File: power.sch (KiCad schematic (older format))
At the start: 70 parts, among them J6 7-17 V IN, Q1 DMP3099L-7, SW7 JS202011SCQN, U1 ICE40HX4K-TQ144, U10 MAX40200AUK, U12 TPS562201, U15 MAX40200AUK, U6 TLV62568APDRLR, U7 TLV62568APDRLR

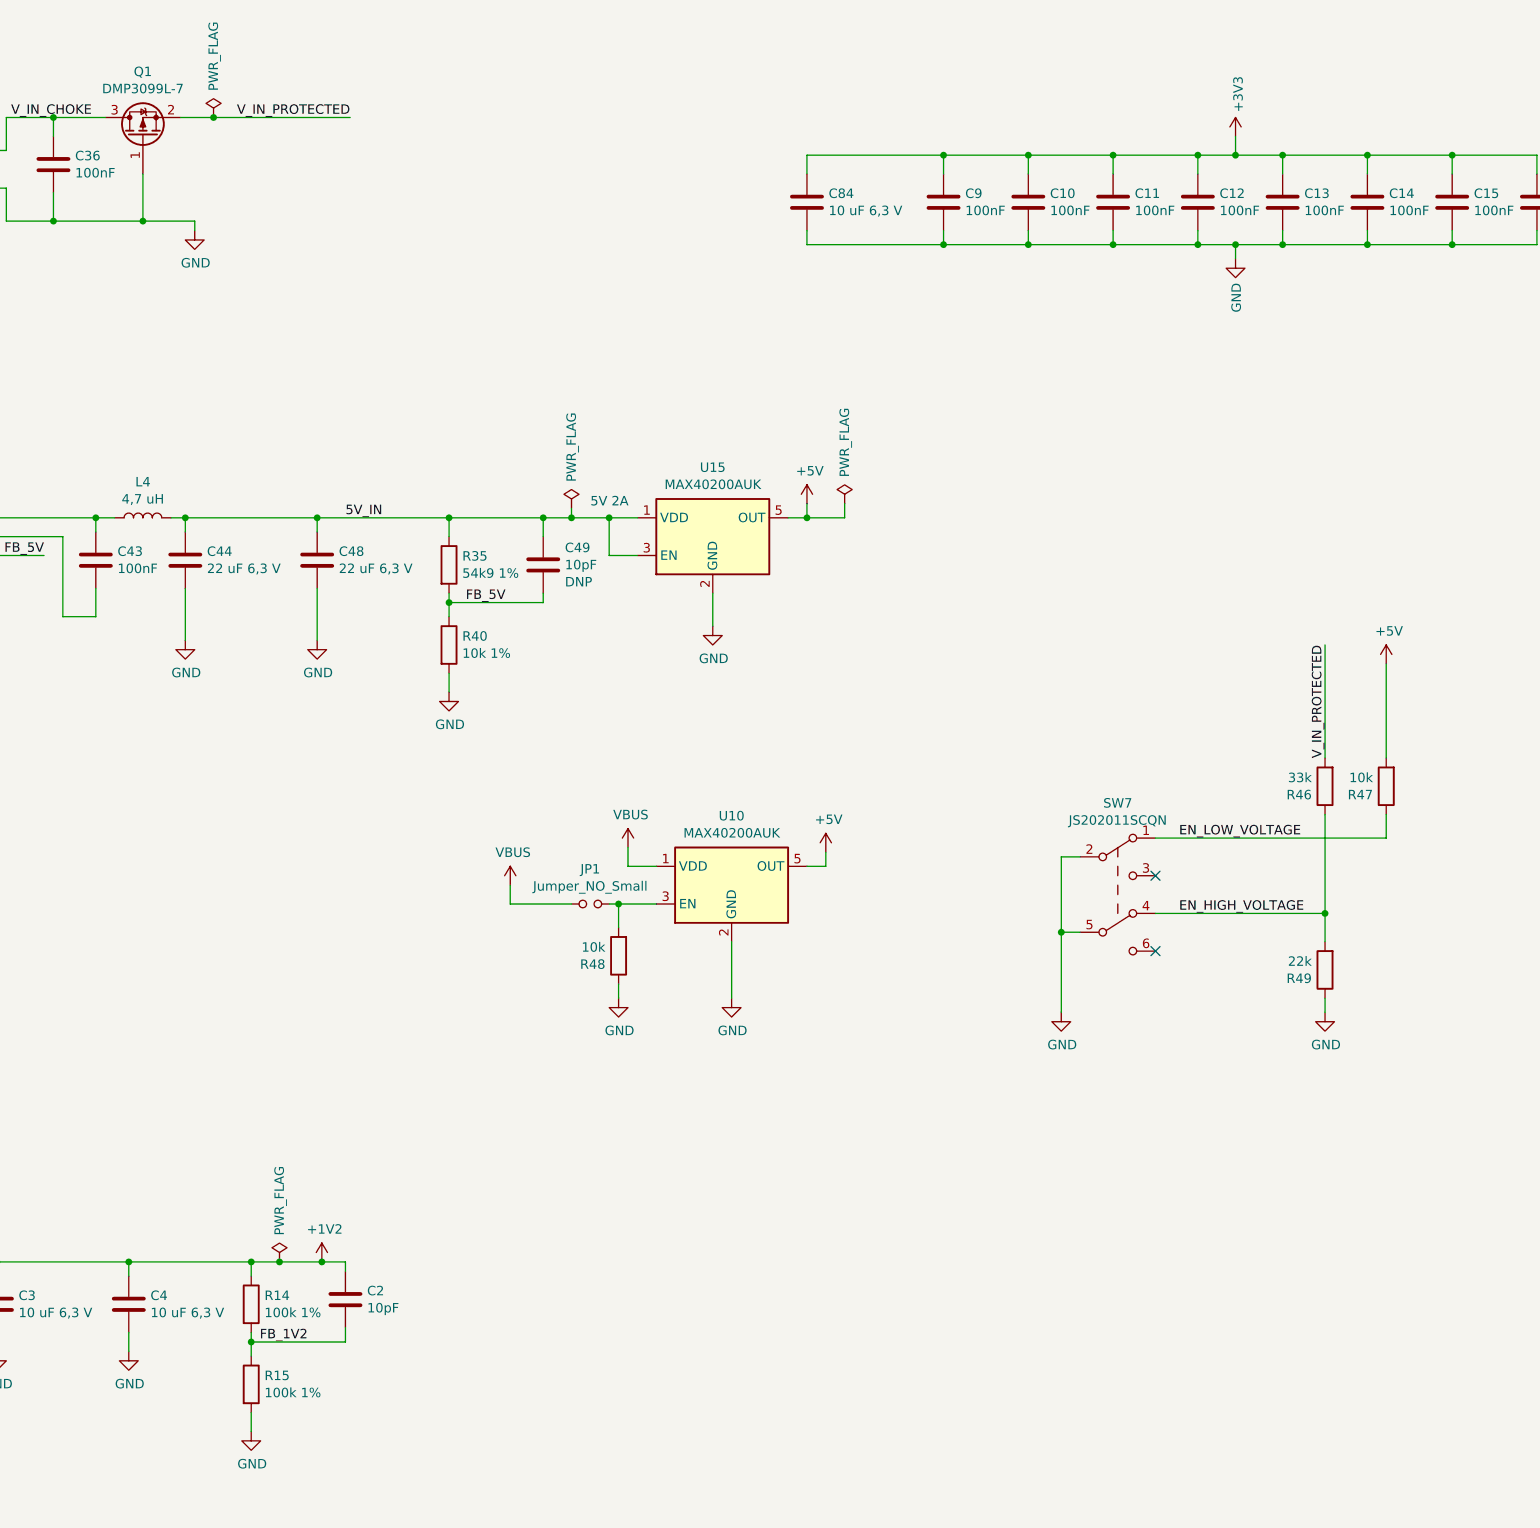
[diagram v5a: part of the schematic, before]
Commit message: Changed power isolation to usb power to use an open drain translator for the reset signals. Continued on routing
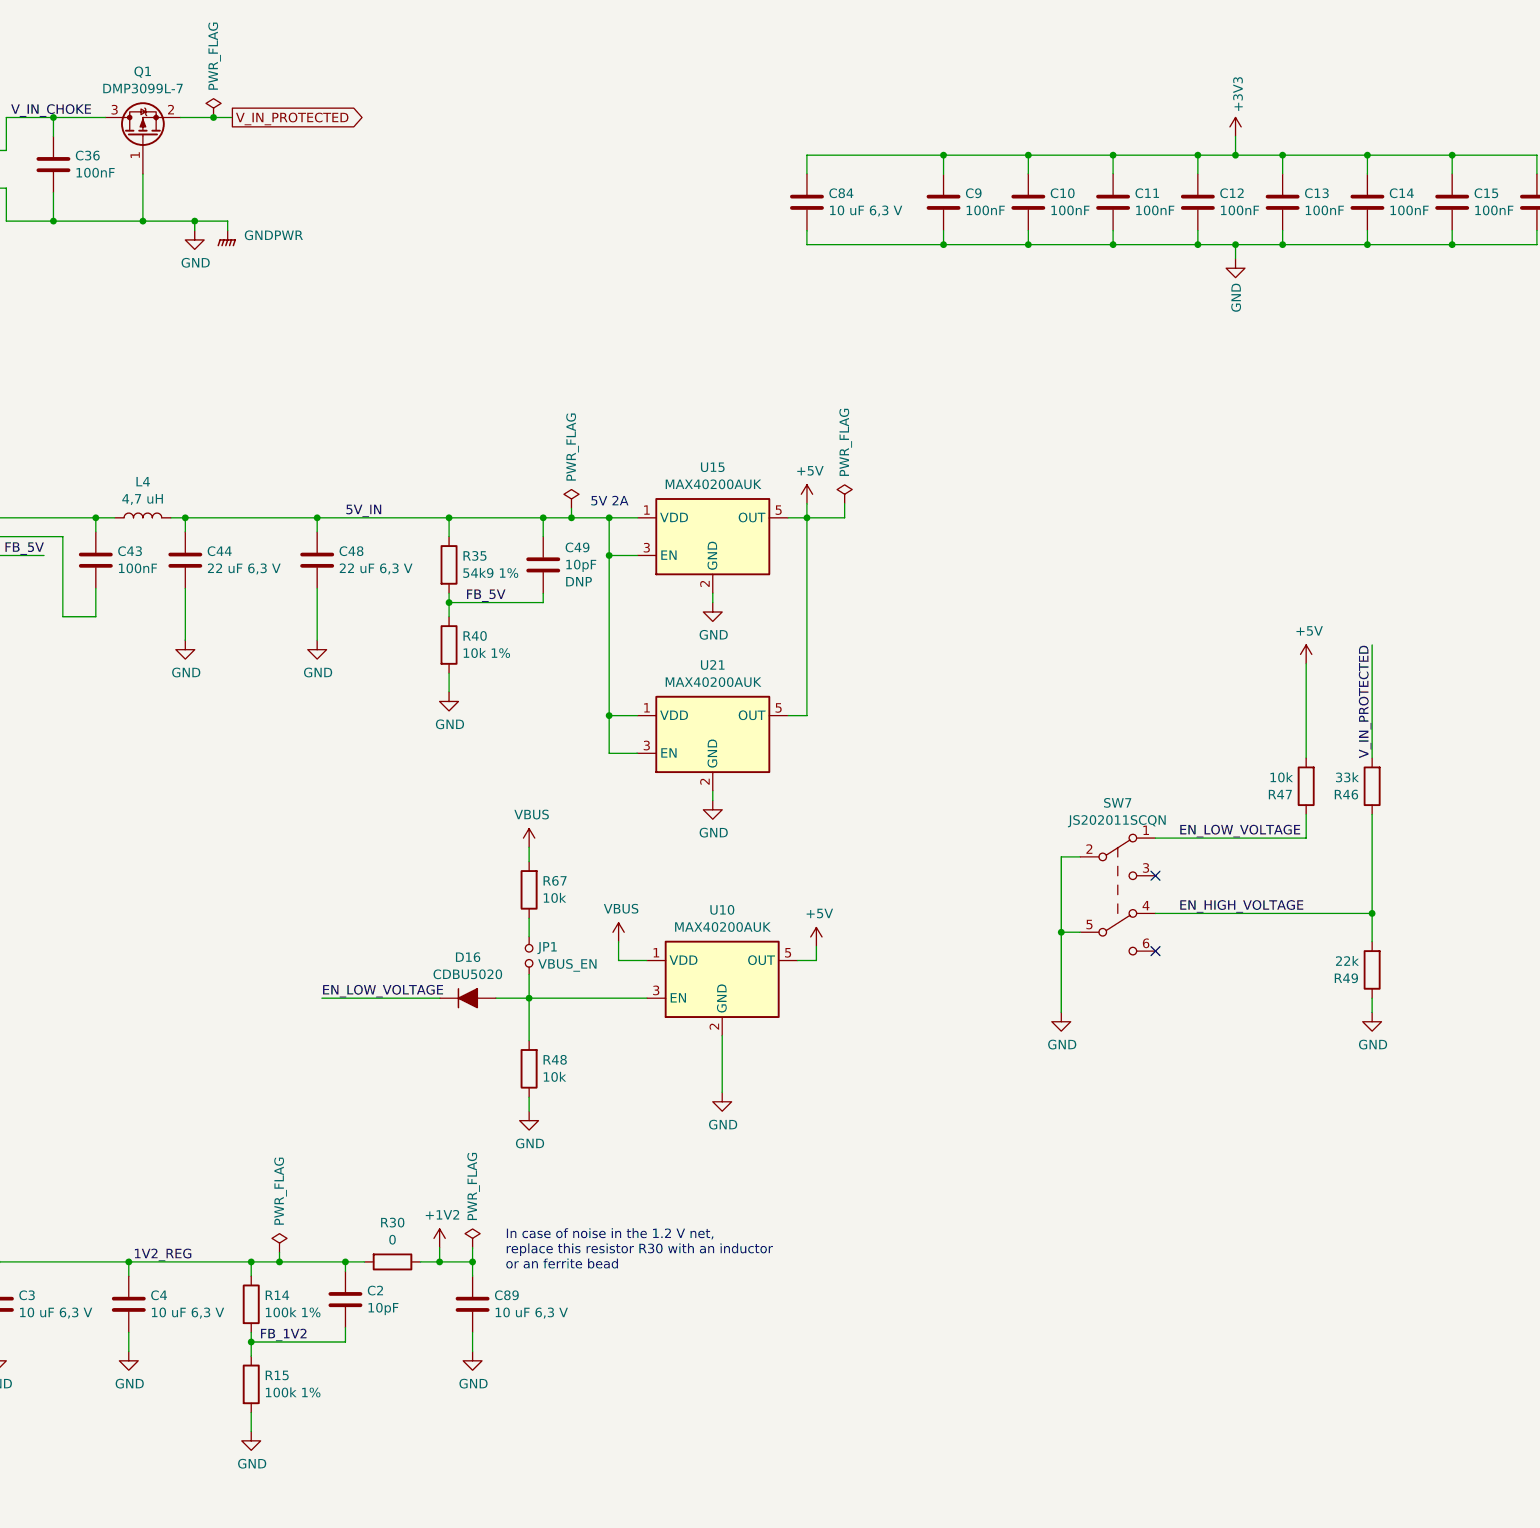
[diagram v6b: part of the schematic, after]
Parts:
- added C89: 10 uF 6,3 V, Capacitor_SMD:C_0603_1608Metric, symbol Device:C
- added D16: CDBU5020, Diode_SMD:D_0603_1608Metric, symbol Device:D_ALT
- added R30: 0, Resistor_SMD:R_0805_2012Metric, symbol Device:R
- added R67: 10k, Resistor_SMD:R_0603_1608Metric, symbol Device:R
- added U21: MAX40200AUK, Package_TO_SOT_SMD:SOT-23-5, symbol Analog_Switch:MAX40200AUK
- JP1: value Jumper_NO_Small -> VBUS_EN
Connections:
- net +1V2: now also C89.1, R30.1; no longer C2.1, C3.1, C4.1, L1.2, R14.1
- net +5V: now also U21.5 (OUT)
- net 5V_IN: now also U21.1 (VDD), U21.3 (EN)
- net EN_LOW_VOLTAGE: now also D16.1 (K)
- net GND: now also C89.2, U21.2 (GND)
- net VBUS: now also R67.2; no longer JP1.1
- net at JP1.2, R48.2, U10.3 (EN): now also D16.2 (A)
- new net: JP1.1, R67.1
- new net 1V2_REG: C2.1, C3.1, C4.1, L1.2, R14.1, R30.2
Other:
- note added: "In case of noise in the 1.2 V net,\nreplace this resistor R30 with an inductor\nor an ferrite bead"
- moved on the sheet: JP1, R46, R47, R48, R49, U10

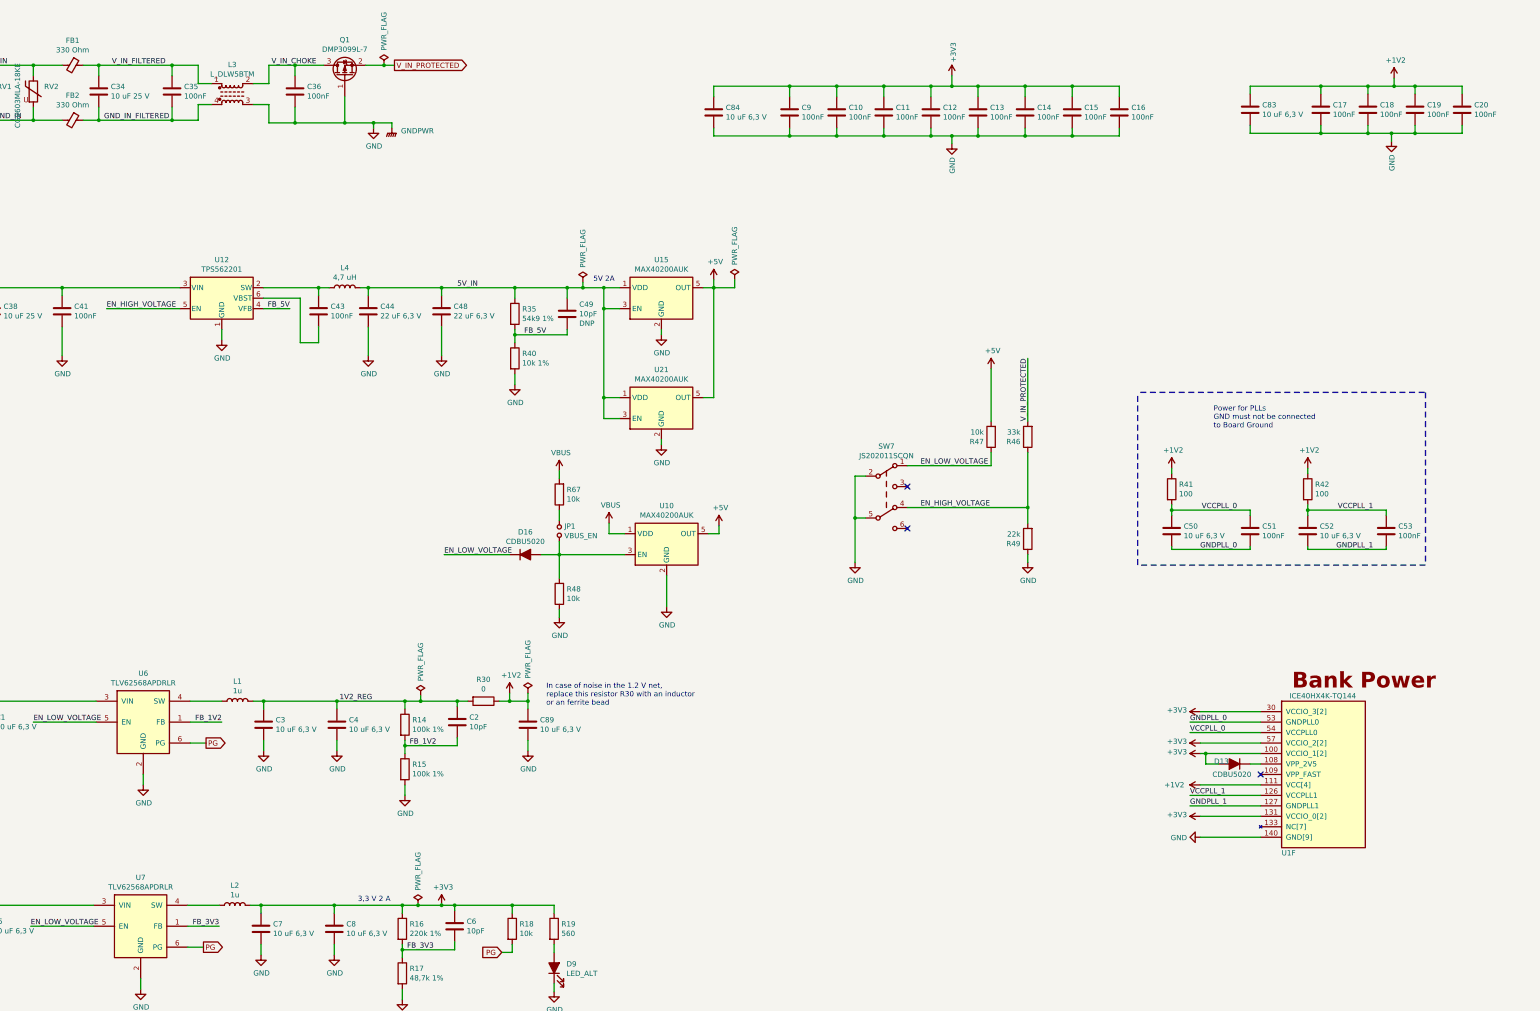
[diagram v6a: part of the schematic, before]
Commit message: Added more BOM information, updated fpga symbol, added some more 3d models
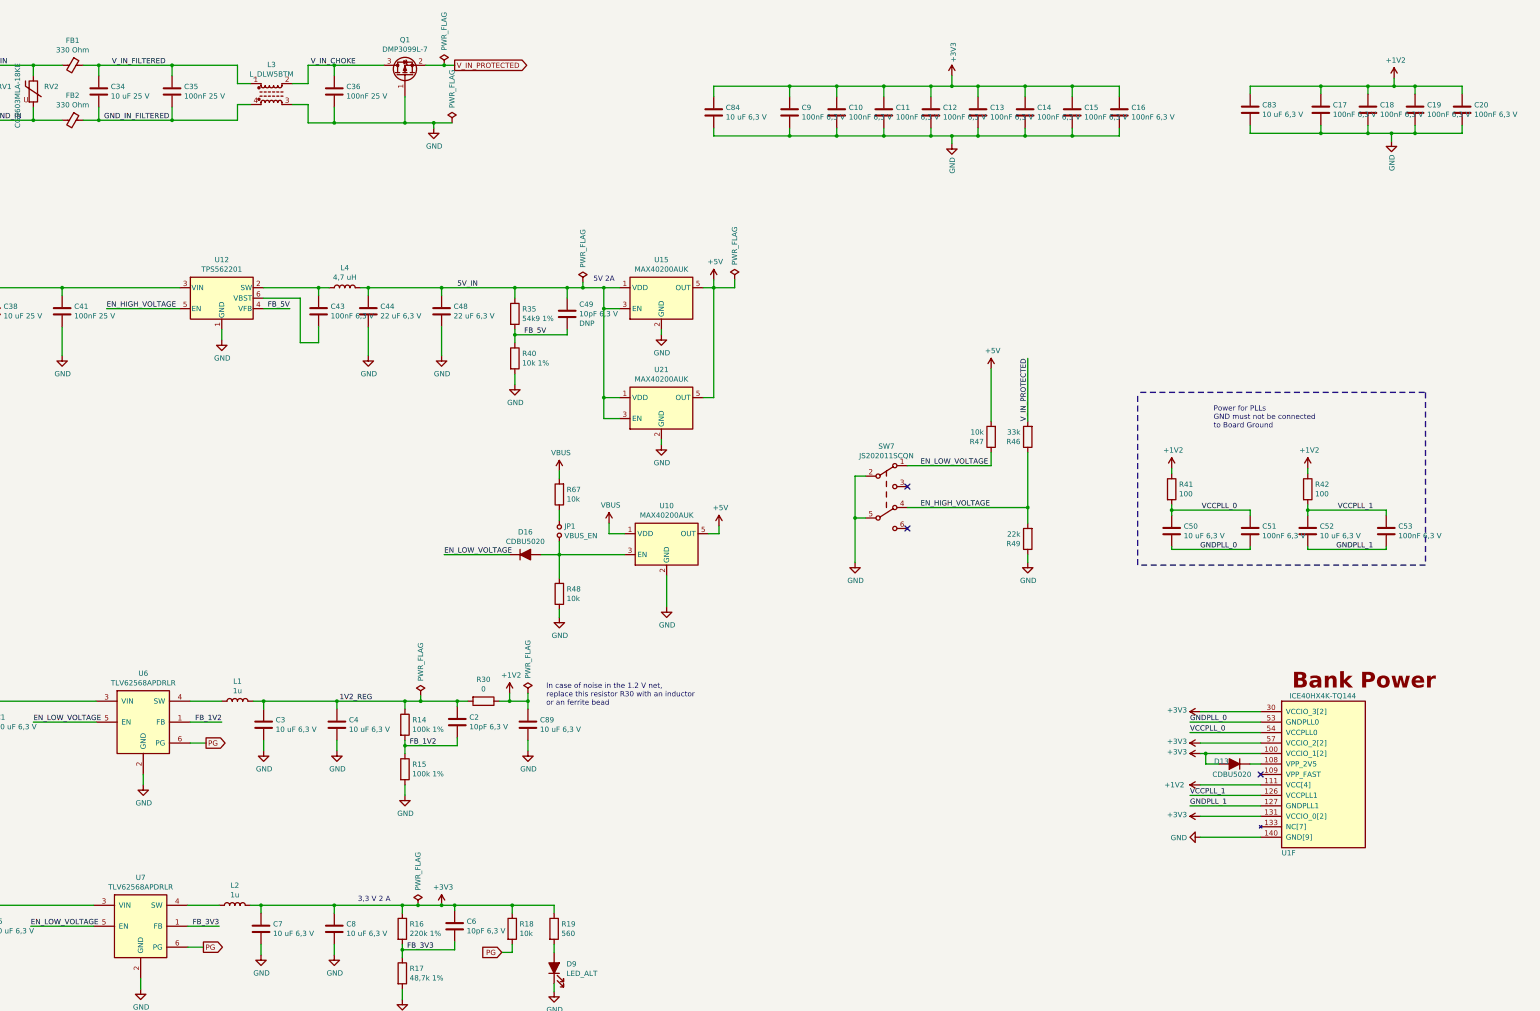
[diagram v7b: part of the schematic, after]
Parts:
- C1, C3, C4, C44, C48, C5, C50, C52, C7, C8, C83, C84, C89, D13, D16: Spec (none) -> Any
- C10, C11, C12, C13, C14, C15, C16, C17, C18, C19, C20, C43, C51, C53, C9: value 100nF -> 100nF 6,3 V; Description (none) -> CAP CER 0.1UF 50V X7R 0603; Digikey (none) -> 1276-1000-1-ND; Mfg Name (none) -> Samsung Electro-Mechanics; Mfg Part Num (none) -> CL10B104KB8NNNC; Spec (none) -> Any
- C2, C49, C6: value 10pF -> 10pF 6,3 V; Description (none) -> CAP CER 10PF 50V C0G/NP0 0603; Digikey (none) -> 1276-1027-1-ND; Mfg Name (none) -> Samsung Electro-Mechanics; Mfg Part Num (none) -> CL10C100JB8NNNC; Spec (none) -> Any
- C35, C36, C41: value 100nF -> 100nF 25 V; Description (none) -> CAP CER 0.1UF 50V X7R 0603; Digikey (none) -> 1276-1000-1-ND; Mfg Name (none) -> Samsung Electro-Mechanics; Mfg Part Num (none) -> CL10B104KB8NNNC; Spec (none) -> Any
- FB1, FB2, L1, L2, L3, L4, Q1, RV1, RV2, SW7, U10, U12, U15, U21: Spec (none) -> Spec
- J6: Description (none) -> ERMINAL BLOCK, SCREW TYPE, 5.08; Digikey (none) -> 102-6203-ND; Mfg Name (none) -> CUI Inc.; Mfg Part Num (none) -> TB007-508-02BE
- U1: Description (none) -> IC FPGA 107 I/O 144TQFP; Digikey (none) -> 220-1572-ND; Mfg Name (none) -> Lattice Semiconductor Corporation; Mfg Part Num (none) -> ICE40HX4K-TQ144; Spec (none) -> Spec
- U6, U7: Description (none) -> IC REG BUCK ADJUSTABLE 1A SOT563; Digikey (none) -> 296-51691-1-ND; Mfg Name (none) -> Texas Instruments; Mfg Part Num (none) -> TLV62568APDRLR; Spec (none) -> Spec
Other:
- moved on the sheet: C36, L3, Q1

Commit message: More BOM Information, more 3d Models
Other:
- note added: "1,2 V 1 A"
- note added: "3,3 V 1 A"
- note added: "Note: Use TLV62568ADRLR for 2 A"
- note removed: "3,3 V 2 A"
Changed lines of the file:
@@
 	-1   0    0    1
 $EndComp
-Text Notes 4825 9075 0    50   ~ 0
-3,3 V 2 A
+Text Notes 3550 8675 0    197  ~ 0
+3,3 V 1 A
 $Comp
 L Device:Varistor RV1
@@
 Text Label 4175 3400 2    50   ~ 0
 FB_5V
-Text Notes 7075 3150 0    50   ~ 0
+Text Notes 5850 2875 0    197  ~ 0
 5V 2A
 Wire Wire Line
@@
 	1    0    0    -1
 $EndComp
+Text Notes 1200 10450 0    100  ~ 0
+Note: Use TLV62568ADRLR for 2 A
+Text Notes 3550 6550 0    197  ~ 0
+1,2 V 1 A
 $EndSCHEMATC
